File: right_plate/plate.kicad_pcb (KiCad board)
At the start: 2 copper layers, 217.2 x 96 mm, 36 parts

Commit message: update plates with asymmetrical pinky stagger
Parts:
- SW16, SW26, SW35, SW36, SW45, SW46: footprint Plate:Switch -> Plate:SwitchDown
- moved SW17 0.50 mm to (206.8, 60.1)
- moved SW18 0.50 mm to (225.5, 63.4)
- moved SW19 0.50 mm to (244.2, 66.7)
- moved SW27 0.50 mm to (203.9, 76.9)
- moved SW28 0.50 mm to (222.6, 80.2)
- moved SW29 0.50 mm to (241.3, 83.5)
- moved SW38 0.50 mm to (219.1, 99.8)
- moved SW47 0.50 mm to (197.4, 113.3)
- moved SW48 0.50 mm to (216.2, 116.6)
- moved SW49 0.50 mm to (234.9, 119.9)
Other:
- outline, holes or cut-outs redrawn

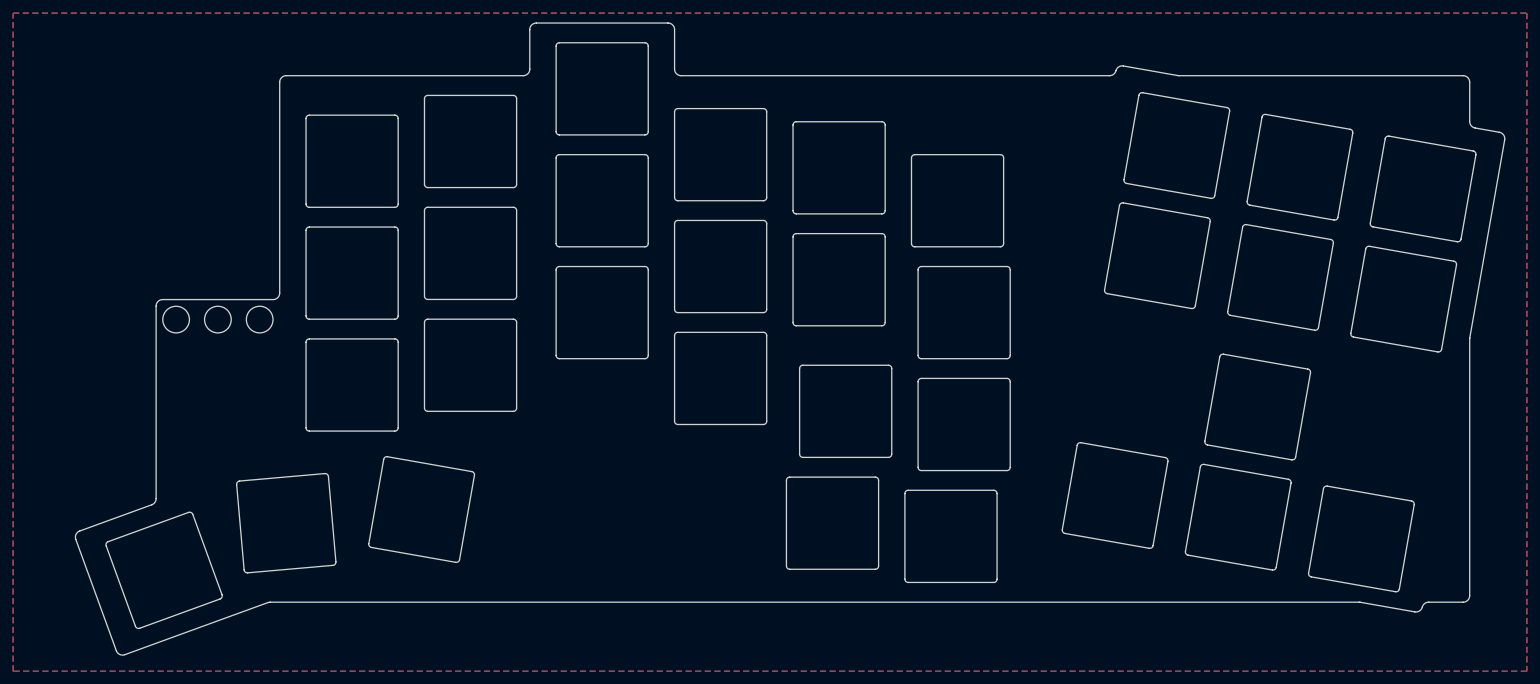
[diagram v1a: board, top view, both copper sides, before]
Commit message: reduce breakoff gap to 1mm
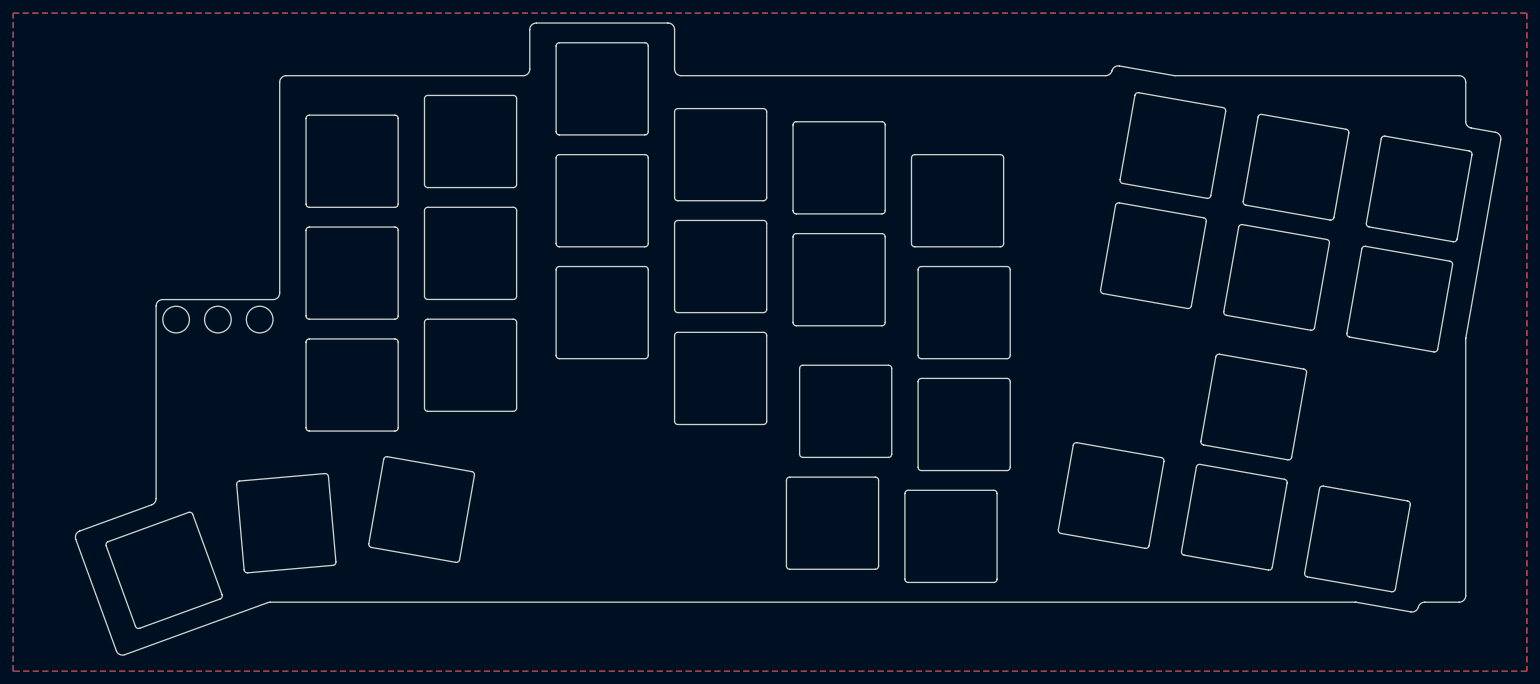
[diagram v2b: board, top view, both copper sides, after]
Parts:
- moved SW19 0.60 mm to (243.6, 66.7)
- moved SW17 0.60 mm to (206.2, 60.1)
- moved SW18 0.60 mm to (224.9, 63.4)
- moved SW27 0.60 mm to (203.3, 76.9)
- moved SW28 0.60 mm to (222.0, 80.2)
- moved SW29 0.60 mm to (240.7, 83.5)
- moved SW38 0.60 mm to (218.5, 99.8)
- moved SW47 0.60 mm to (196.8, 113.3)
- moved SW48 0.60 mm to (215.6, 116.6)
- moved SW49 0.60 mm to (234.3, 119.9)
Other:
- board size 217.2 x 96 mm -> 216.6 x 96 mm
